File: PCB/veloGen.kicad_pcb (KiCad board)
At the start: 2 copper layers, 67 x 24 mm, 40 parts, among them J1 Conn_01x06, J2 Gen. IN, J3 Bat, Q3 STL6N3LLH6, T1 MSD1260, U1 ESP-WROOM-32, U4 MAX8881, U5 MCP1630

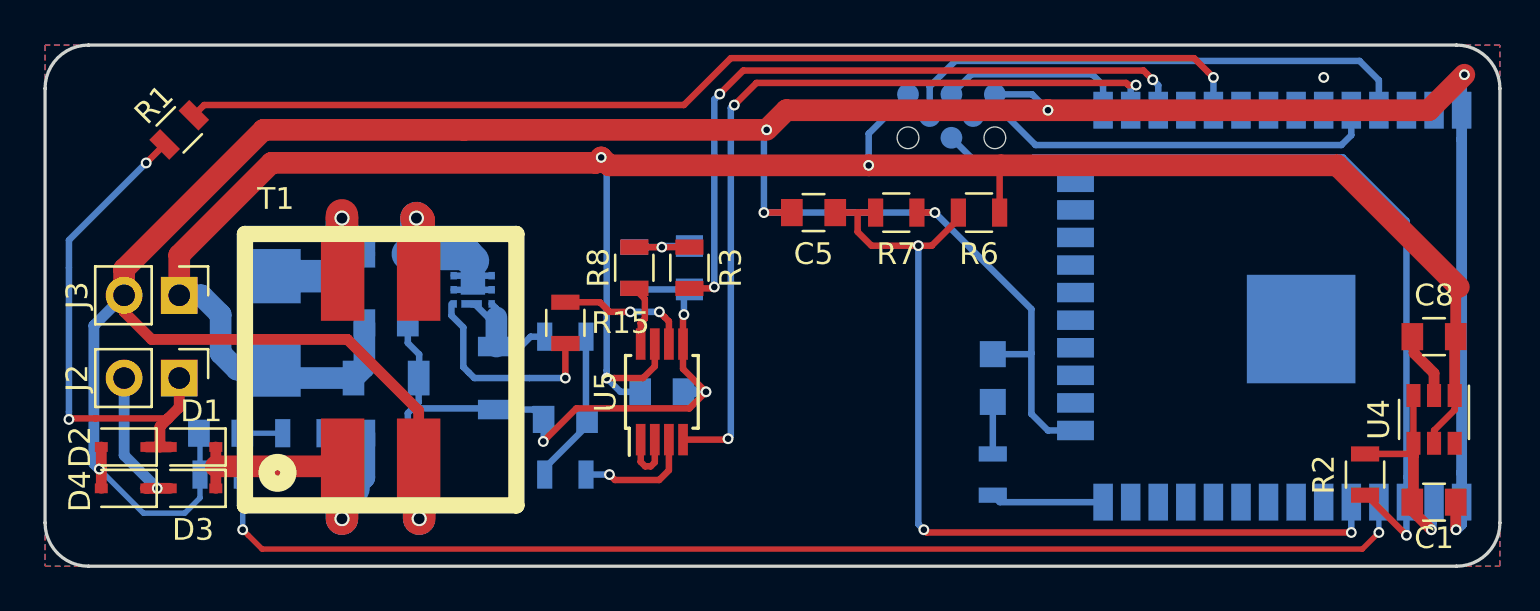
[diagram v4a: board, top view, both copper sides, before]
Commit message: Added batery current sense
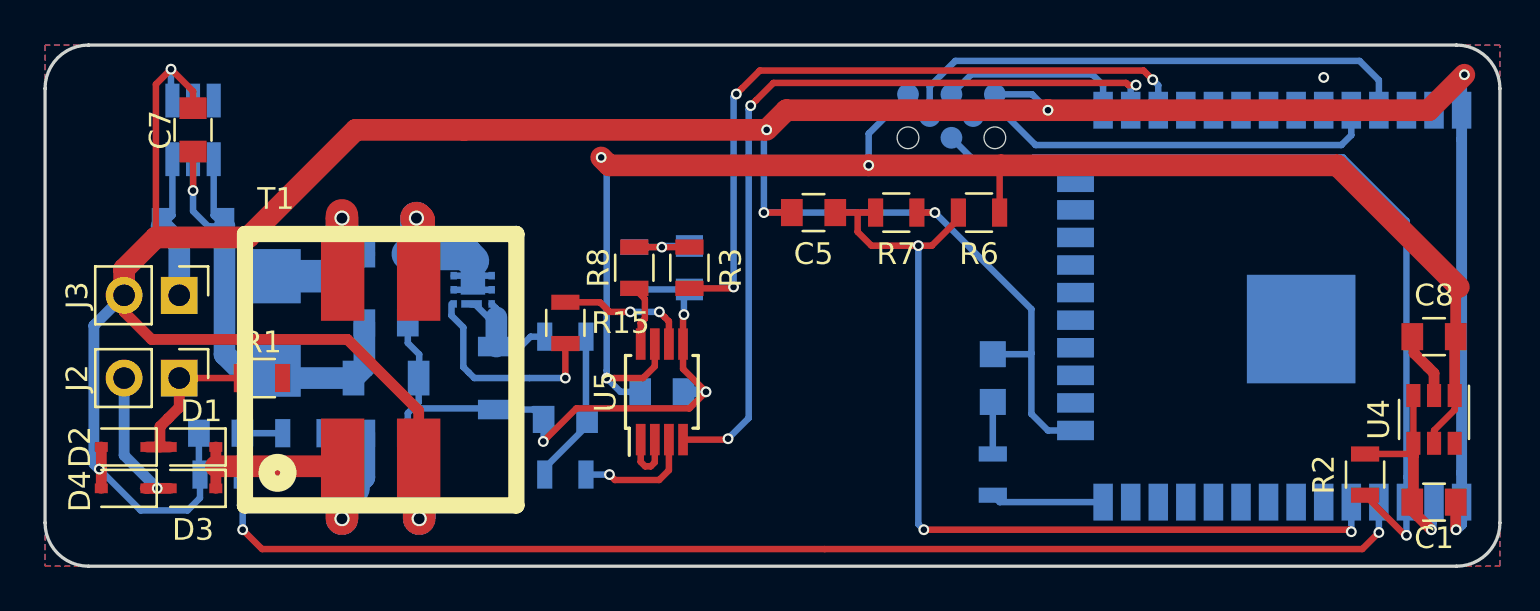
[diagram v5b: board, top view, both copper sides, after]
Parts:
- added C7: 470n, Capacitors_SMD:C_0805, F.Cu at (43.8, 128.9)
- added R9: 100m, Resistors_SMD:R_1206, B.Cu at (43.8, 133.3)
- added U2: TS1101, TO_SOT_Packages_SMD:SOT-23-6_Handsoldering, B.Cu at (43.8, 128.9)
- moved R1 12.0 mm to (47.0, 140.3), turned to 0 degrees
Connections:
- J3 pad 1: +BATT -> Net-(J3-Pad1)
- U1 pad 10: Net-(U1-Pad10) -> /IBattSign
- U1 pad 6: Net-(U1-Pad6) -> /IBatt
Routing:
- net /speedPulse: track 49.9 -> 0.00 mm, vias 1 -> 0
- net Net-(D1-Pad2): track 24.8 -> 8.55 mm, vias 2 -> 0
- net +BATT: track 107.9 -> 95.7 mm, vias 3 -> 4
- net GND: track 199.5 -> 211.1 mm, vias 12 -> 13
- net Net-(J3-Pad1): track 0.00 -> 6.81 mm
